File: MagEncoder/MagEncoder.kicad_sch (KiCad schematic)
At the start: 32 parts, among them J1 Main, J2 Debug, J3 Thermistor, U1 ADM4852, U2 STM32G4A1KEU4, U3 LP5907MFX-3.3, U4 MA730

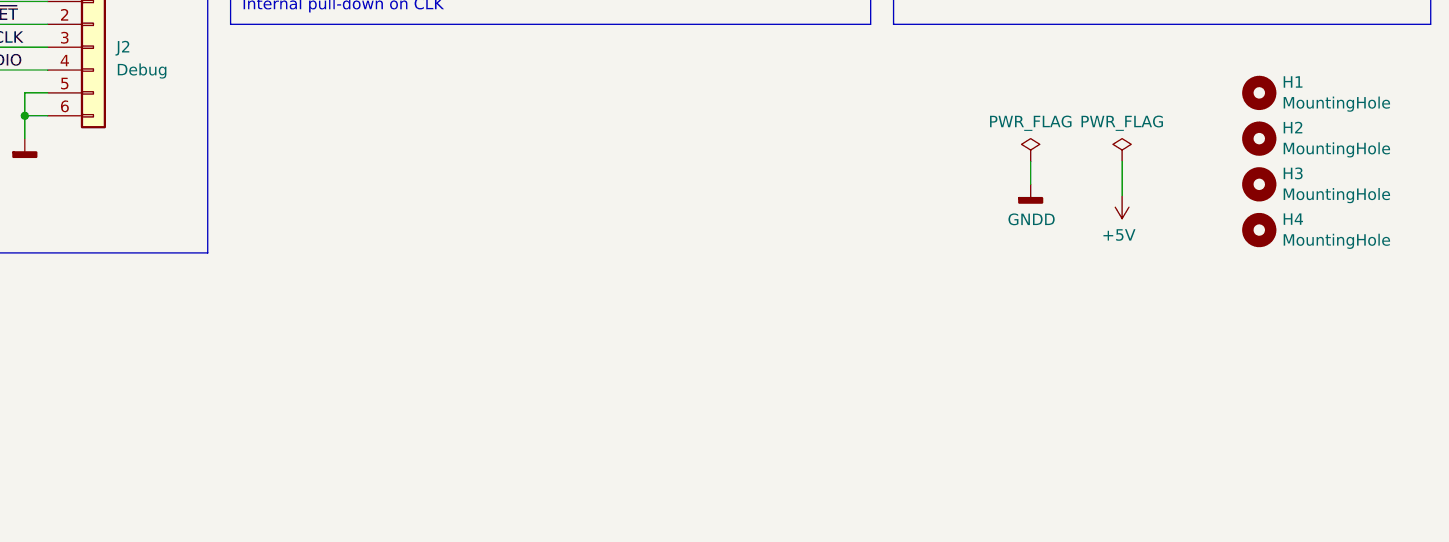
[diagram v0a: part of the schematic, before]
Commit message: Add RGB LED
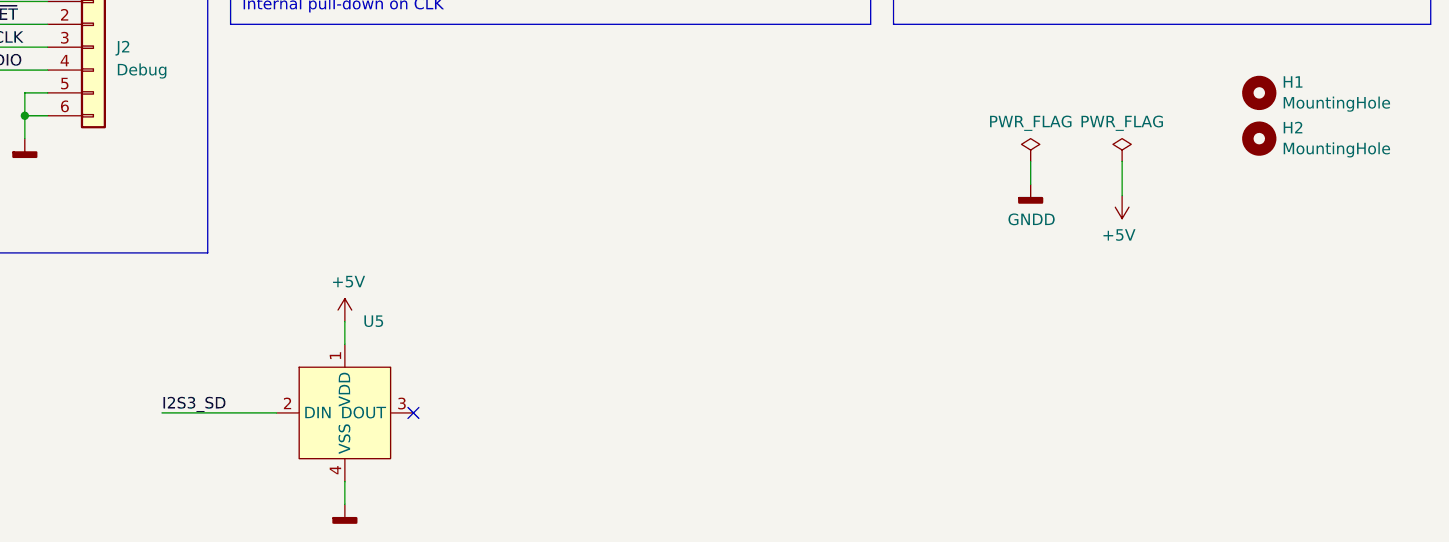
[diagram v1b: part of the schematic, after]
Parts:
- removed H3, H4: MountingHole, MountingHole:MountingHole_3mm, symbol Mechanical:MountingHole
- added U5: (no value), symbol Wetmelon:LTST-E263CEGBK
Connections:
- net +5V: now also U5.1 (VDD)
- net GNDD: now also U5.4 (VSS)
- net I2S3_SD: now also U5.2 (DIN)
- no-connect marks 16 -> 17
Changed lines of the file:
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@@
   (no_connect (at 151.13 115.57))
   (no_connect (at 176.53 107.95))
+  (no_connect (at 142.24 176.53))
   (no_connect (at 176.53 113.03))
   (no_connect (at 62.23 88.9))
@@
     (stroke (width 0) (type default) (color 0 0 0 0))
   )
+  (wire (pts (xy 127 176.53) (xy 114.3 176.53))
+    (stroke (width 0) (type default) (color 0 0 0 0))
+  )
   (wire (pts (xy 166.37 125.73) (xy 166.37 123.19))
     (stroke (width 0) (type default) (color 0 0 0 0))
@@
     (stroke (width 0) (type default) (color 0 0 0 0))
   )
+  (wire (pts (xy 134.62 166.37) (xy 134.62 168.91))
+    (stroke (width 0) (type default) (color 0 0 0 0))
+  )
   (wire (pts (xy 99.06 143.51) (xy 101.6 143.51))
     (stroke (width 0) (type default) (color 0 0 0 0))
@@
   )
   (polyline (pts (xy 255.27 82.55) (xy 195.58 82.55))
+    (stroke (width 0) (type default) (color 0 0 0 0))
+  )
+  (wire (pts (xy 134.62 184.15) (xy 134.62 186.69))
     (stroke (width 0) (type default) (color 0 0 0 0))
   )
@@
   )
   (text "Debug IO" (at 87.63 119.38 0)
+    (effects (font (size 1.27 1.27)) (justify left bottom))
+  )
+  (label "I2S3_SD" (at 114.3 176.53 0)
     (effects (font (size 1.27 1.27)) (justify left bottom))
   )
@@
     (pin "1")
   )
+  (symbol (lib_id "power:GNDD") (at 134.62 186.69 0) (unit 1)
+    (in_bom yes) (on_board yes)
+    (property "Reference" "#PWR026" (id 0) (at 134.62 193.04 0)
+      (effects (font (size 1.27 1.27)) hide)
+    )
+    (property "Value" "GNDD" (id 1) (at 134.7216 190.627 0)
+      (effects (font (size 1.27 1.27)) hide)
+    )
+    (property "Footprint" "" (id 2) (at 134.62 186.69 0)
+      (effects (font (size 1.27 1.27)) hide)
+    )
+    (property "Datasheet" "" (id 3) (at 134.62 186.69 0)
+      (effects (font (size 1.27 1.27)) hide)
+    )
+    (pin "1")
+  )
   (symbol (lib_id "Regulator_Linear:LP5907MFX-3.3") (at 219.71 104.14 0) (unit 1)
     (in_bom yes) (on_board yes) (fields_autoplaced)
@@
     )
     (pin "1")
+  )
+  (symbol (lib_id "Wetmelon:LTST-E263CEGBK") (at 134.62 176.53 0) (unit 1)
+    (in_bom yes) (on_board yes) (fields_autoplaced)
+    (property "Reference" "U5" (id 0) (at 136.6394 166.37 0)
+      (effects (font (size 1.27 1.27)) (justify left))
+    )
+    (property "Value" "" (id 1) (at 136.6394 168.91 0)
+      (effects (font (size 1.27 1.27)) (justify left))
+    )
+    (property "Footprint" "" (id 2) (at 134.62 176.53 0)
+      (effects (font (size 1.27 1.27)) hide)
+    )
+    (property "Datasheet" "" (id 3) (at 134.62 176.53 0)
+      (effects (font (size 1.27 1.27)) hide)
+    )
+    (pin "1")
+    (pin "2")
+    (pin "3")
+    (pin "4")
   )
   (symbol (lib_id "power:GNDD") (at 238.76 39.37 0) (unit 1)
@@
     (pin "1")
   )
-  (symbol (lib_id "Mechanical:MountingHole") (at 236.22 151.13 0) (unit 1)
-    (in_bom yes) (on_board yes)
-    (property "Reference" "H3" (id 0) (at 238.76 149.9616 0)
-      (effects (font (size 1.27 1.27)) (justify left))
-    )
-    (property "Value" "MountingHole" (id 1) (at 238.76 152.273 0)
-      (effects (font (size 1.27 1.27)) (justify left))
-    )
-    (property "Footprint" "MountingHole:MountingHole_3mm" (id 2) (at 236.22 151.13 0)
-      (effects (font (size 1.27 1.27)) hide)
-    )
-    (property "Datasheet" "~" (id 3) (at 236.22 151.13 0)
-      (effects (font (size 1.27 1.27)) hide)
-    )
-  )
   (symbol (lib_id "power:+3.3V") (at 63.5 27.94 0) (unit 1)
     (in_bom yes) (on_board yes)
@@
     (pin "1")
   )
+  (symbol (lib_id "power:+5V") (at 134.62 166.37 0) (unit 1)
+    (in_bom yes) (on_board yes)
+    (property "Reference" "#PWR025" (id 0) (at 134.62 170.18 0)
+      (effects (font (size 1.27 1.27)) hide)
+    )
+    (property "Value" "+5V" (id 1) (at 135.001 161.9758 0))
+    (property "Footprint" "" (id 2) (at 134.62 166.37 0)
+      (effects (font (size 1.27 1.27)) hide)
+    )
+    (property "Datasheet" "" (id 3) (at 134.62 166.37 0)
+      (effects (font (size 1.27 1.27)) hide)
+    )
+    (pin "1")
+  )
   (symbol (lib_id "Device:C_Small") (at 101.6 88.9 0) (unit 1)
     (in_bom yes) (on_board yes)
@@
     (pin "1")
     (pin "2")
-  )
-  (symbol (lib_id "Mechanical:MountingHole") (at 236.22 156.21 0) (unit 1)
-    (in_bom yes) (on_board yes)
-    (property "Reference" "H4" (id 0) (at 238.76 155.0416 0)
-      (effects (font (size 1.27 1.27)) (justify left))
-    )
-    (property "Value" "MountingHole" (id 1) (at 238.76 157.353 0)
-      (effects (font (size 1.27 1.27)) (justify left))
-    )
-    (property "Footprint" "MountingHole:MountingHole_3mm" (id 2) (at 236.22 156.21 0)
-      (effects (font (size 1.27 1.27)) hide)
-    )
-    (property "Datasheet" "~" (id 3) (at 236.22 156.21 0)
-      (effects (font (size 1.27 1.27)) hide)
-    )
   )
   (symbol (lib_id "Connector:TestPoint") (at 233.68 78.74 270) (unit 1)
@@
       (reference "#PWR024") (unit 1) (value "+5V") (footprint "")
     )
+    (path "/95a2dace-e27e-4fcc-aa01-31cd0391409f"
+      (reference "#PWR025") (unit 1) (value "+5V") (footprint "")
+    )
+    (path "/34ea93bf-8ea9-4739-8fd7-f3fd8a5d4efc"
+      (reference "#PWR026") (unit 1) (value "GNDD") (footprint "")
+    )
     (path "/00000000-0000-0000-0000-00005f97c619"
       (reference "C1") (unit 1) (value "100nF") (footprint "Capacitor_SMD:C_0402_1005Metric")
@@
       (reference "H2") (unit 1) (value "MountingHole") (footprint "MountingHole:MountingHole_3mm")
     )
-    (path "/8a61e2f2-3716-44c4-b12c-058a496def9b"
-      (reference "H3") (unit 1) (value "MountingHole") (footprint "MountingHole:MountingHole_3mm")
-    )
-    (path "/a52f6e08-f34e-4095-832d-e87ac0e56f92"
-      (reference "H4") (unit 1) (value "MountingHole") (footprint "MountingHole:MountingHole_3mm")
-    )
     (path "/f6f03c69-3ab7-43e0-baed-8d80062ab2d2"
       (reference "J1") (unit 1) (value "Main") (footprint "Connector_Molex:Molex_CLIK-Mate_502585-0670_1x06-1MP_P1.50mm_Horizontal")
@@
       (reference "U4") (unit 1) (value "MA730") (footprint "Package_DFN_QFN:QFN-16-1EP_3x3mm_P0.5mm_EP1.7x1.7mm")
     )
-  )
+    (path "/4436cebc-fae4-4e6c-9d1c-4628107502b5"
+      (reference "U5") (unit 1) (value "LTST-E263CEGBK") (footprint "ODrive_KiCad:LTST")
+    )
+  )
